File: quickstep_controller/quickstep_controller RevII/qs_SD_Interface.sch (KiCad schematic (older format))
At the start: 17 parts, among them J201 SD_Card, U201 TS3A27518E, U202 SN74LVC1G3157DCK3

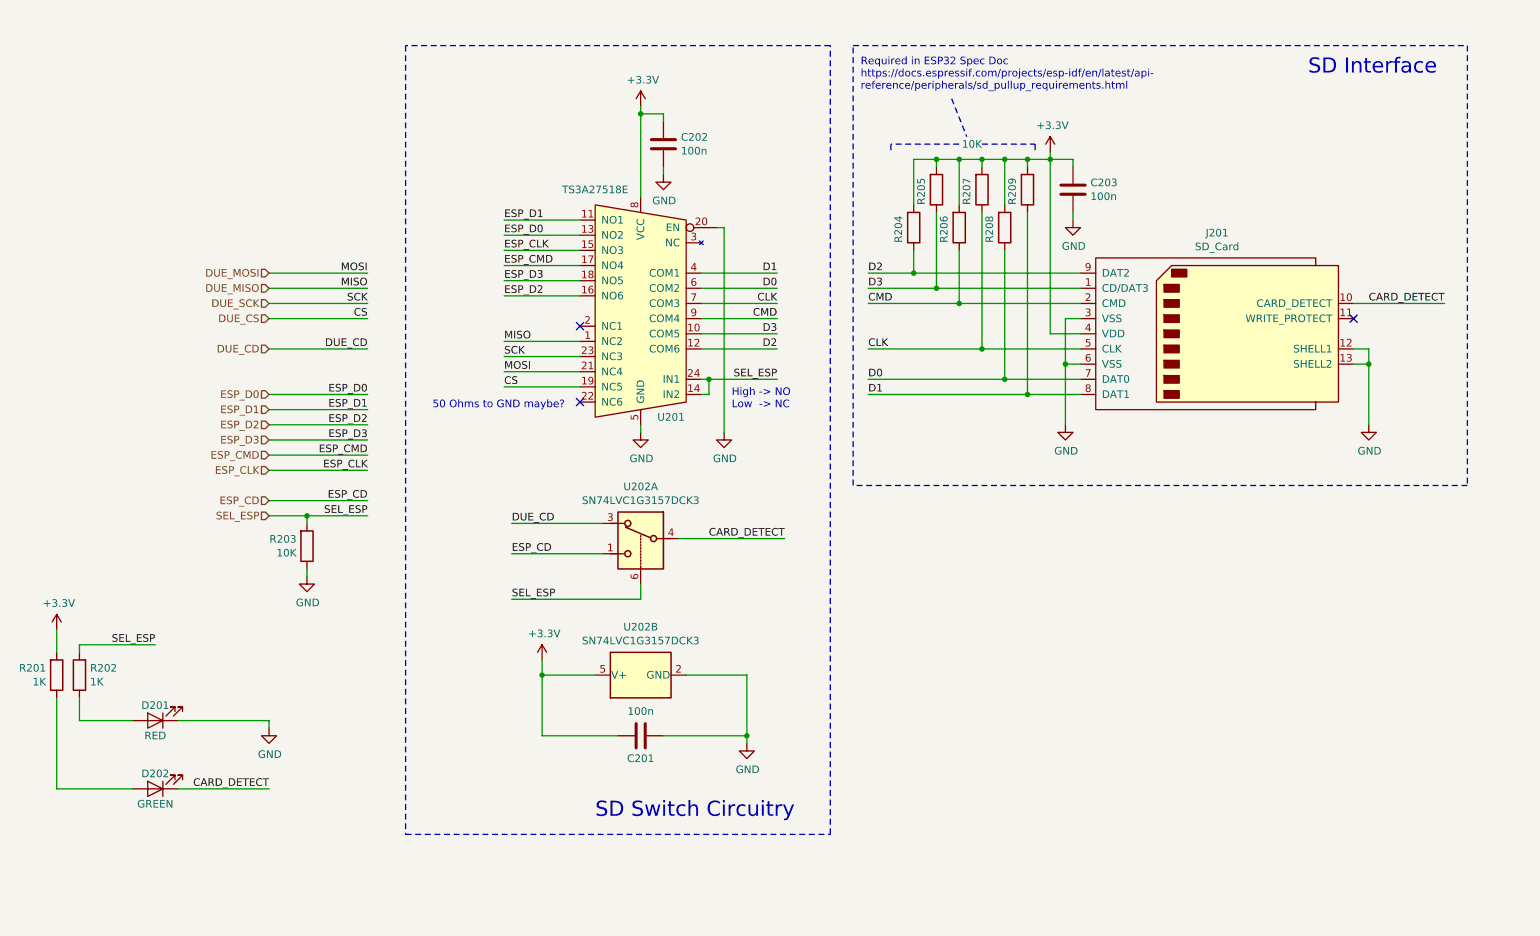
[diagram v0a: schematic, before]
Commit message: Messing around with direct SD-MMC upload; hardware changes required and messing around with ESP3D
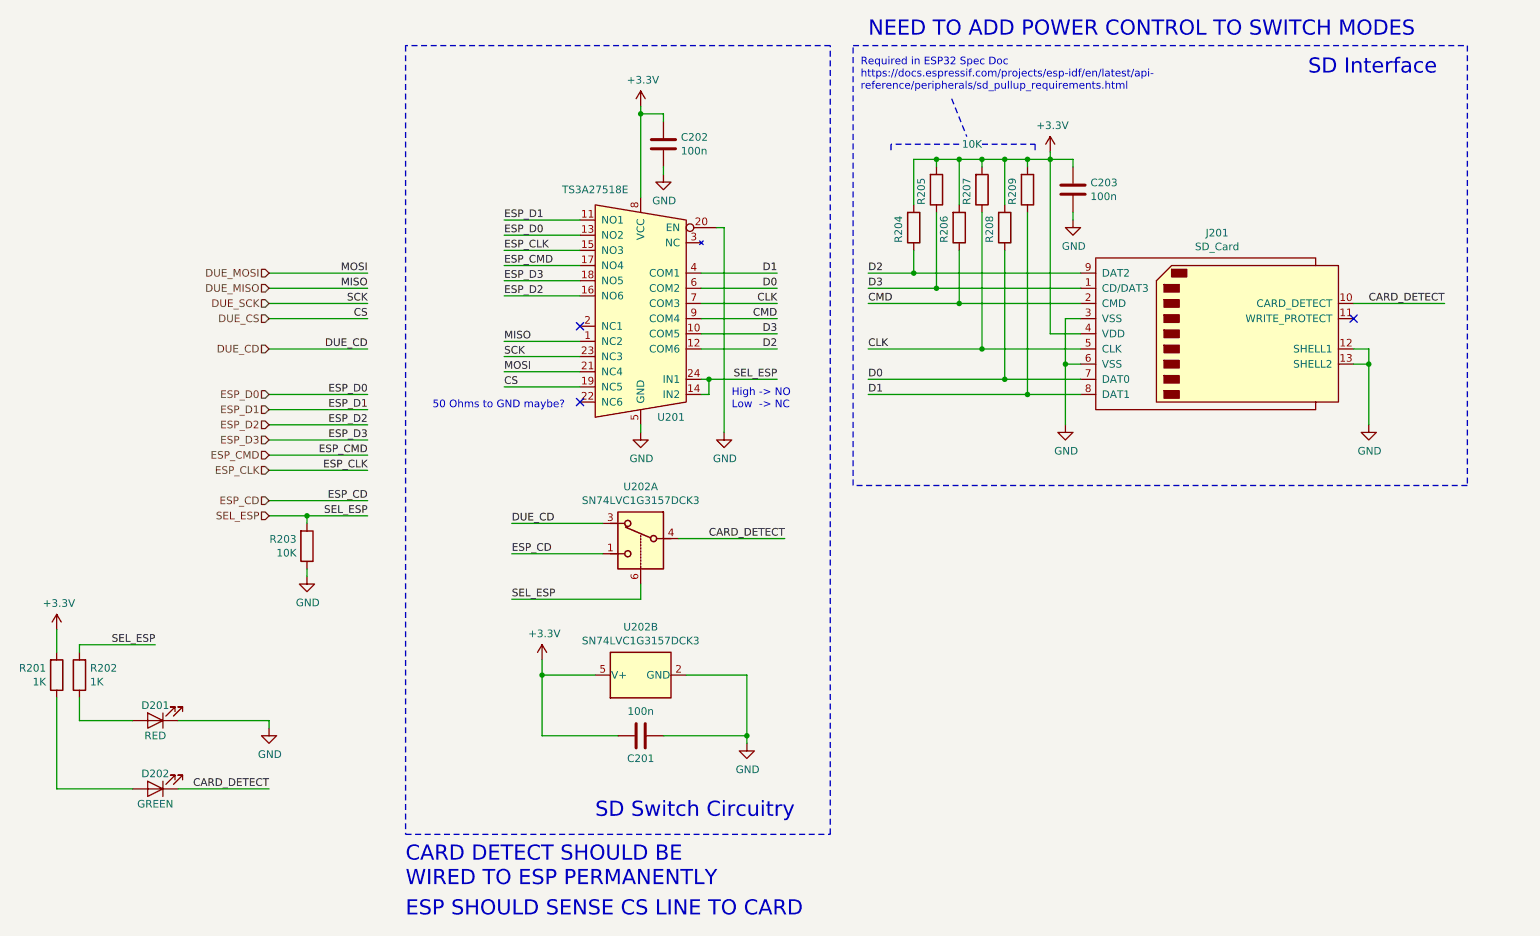
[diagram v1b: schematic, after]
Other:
- note added: "CARD DETECT SHOULD BE \nWIRED TO ESP PERMANENTLY"
- note added: "ESP SHOULD SENSE CS LINE TO CARD"
- note added: "NEED TO ADD POWER CONTROL TO SWITCH MODES"
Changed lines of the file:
@@
 EESchema Schematic File Version 4
+LIBS:quickstep_controller RevII-cache
 EELAYER 30 0
 EELAYER END
@@
 Wire Wire Line
 	2750 3400 3400 3400
+Text Notes 6700 1550 0    100  ~ 0
+NEED TO ADD POWER CONTROL TO SWITCH MODES
+Text Notes 3650 7150 0    100  ~ 0
+CARD DETECT SHOULD BE \nWIRED TO ESP PERMANENTLY
+Text Notes 3650 7350 0    100  ~ 0
+ESP SHOULD SENSE CS LINE TO CARD
 $EndSCHEMATC
